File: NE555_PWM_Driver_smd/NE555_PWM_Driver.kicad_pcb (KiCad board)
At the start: 2 copper layers, 43 x 51 mm, 14 parts, among them J1 Input, J2 Output, Q1 IRFZ44N, U1 NE555P

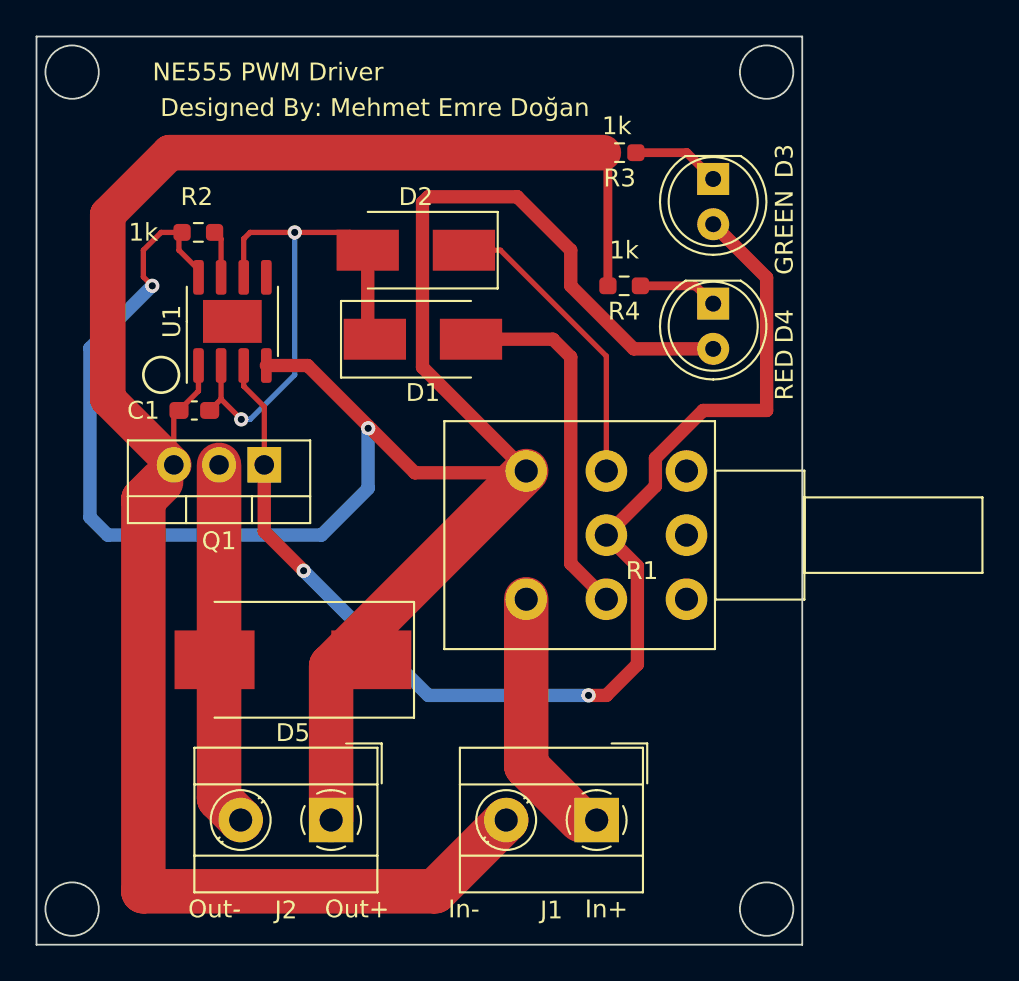
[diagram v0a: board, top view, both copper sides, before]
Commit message: filled top plane with ground
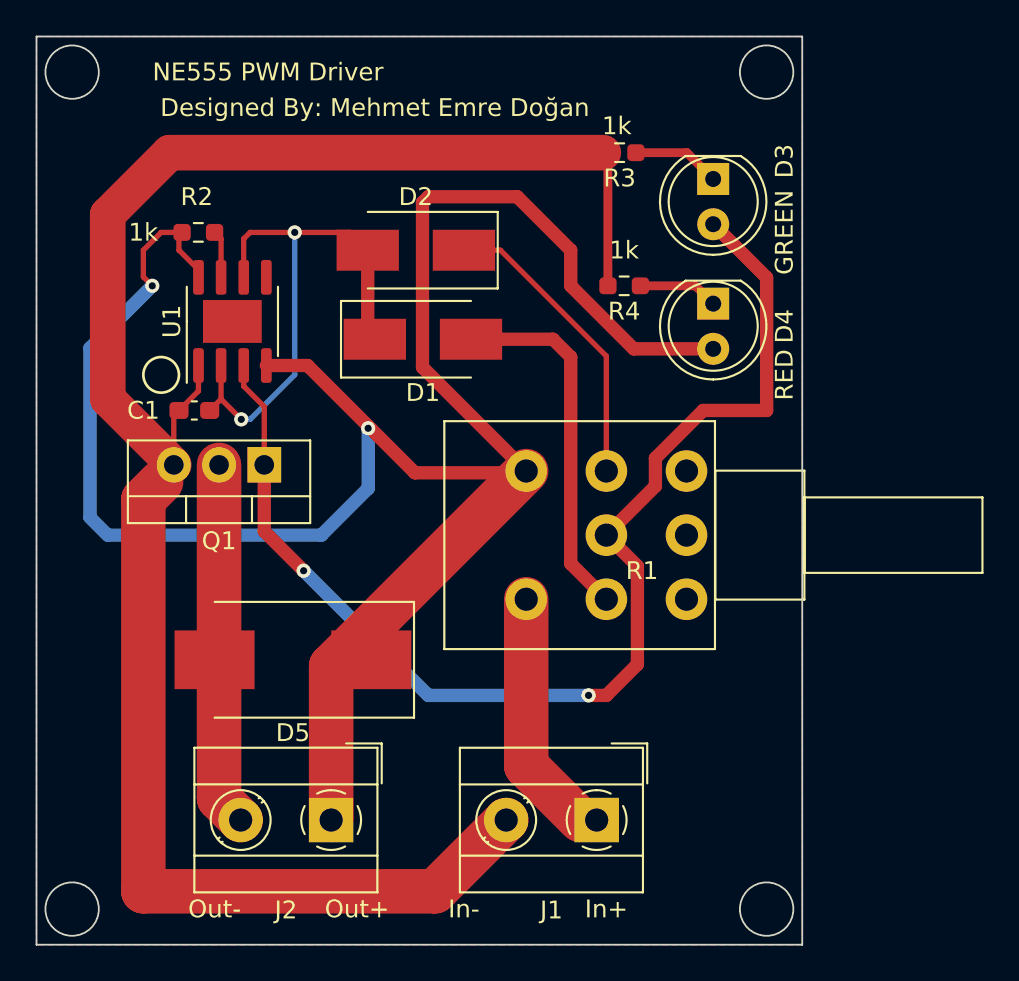
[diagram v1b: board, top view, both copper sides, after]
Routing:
- added copper zone on F.Cu, net GND
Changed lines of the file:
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@@
   (segment (start 166.365 87.365) (end 166 87) (width 0.3) (layer "F.Cu") (net 11))
   (segment (start 166.365 89.525) (end 166.365 87.365) (width 0.3) (layer "F.Cu") (net 11))
+  (zone (net 2) (net_name "GND") (layer "F.Cu") (hatch edge 0.508)
+    (connect_pads (clearance 0.508))
+    (min_thickness 0.254) (filled_areas_thickness no)
+    (fill yes (thermal_gap 0.508) (thermal_bridge_width 0.508))
+    (polygon
+      (pts
+        (xy 199 127)
+        (xy 156 127)
+        (xy 156 76)
+        (xy 199 76)
+      )
+    )
+  )
 )
